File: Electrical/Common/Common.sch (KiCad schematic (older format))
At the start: 40 parts, among them J101 4PostTerm, J102 2PostTerm, J103 2PostTerm, J104 Conn_01x03, J105 01x02, J106 Conn_01x02, J107 01x04, J108 01x04, J109 01x04-1V8, J110 01x04-3v3, U101 ACS712ELCTR-05B-T, U102 ACS712ELCTR-05B-T, U103 LM2576HVS-ADJ, U104 LM2576HVS-ADJ

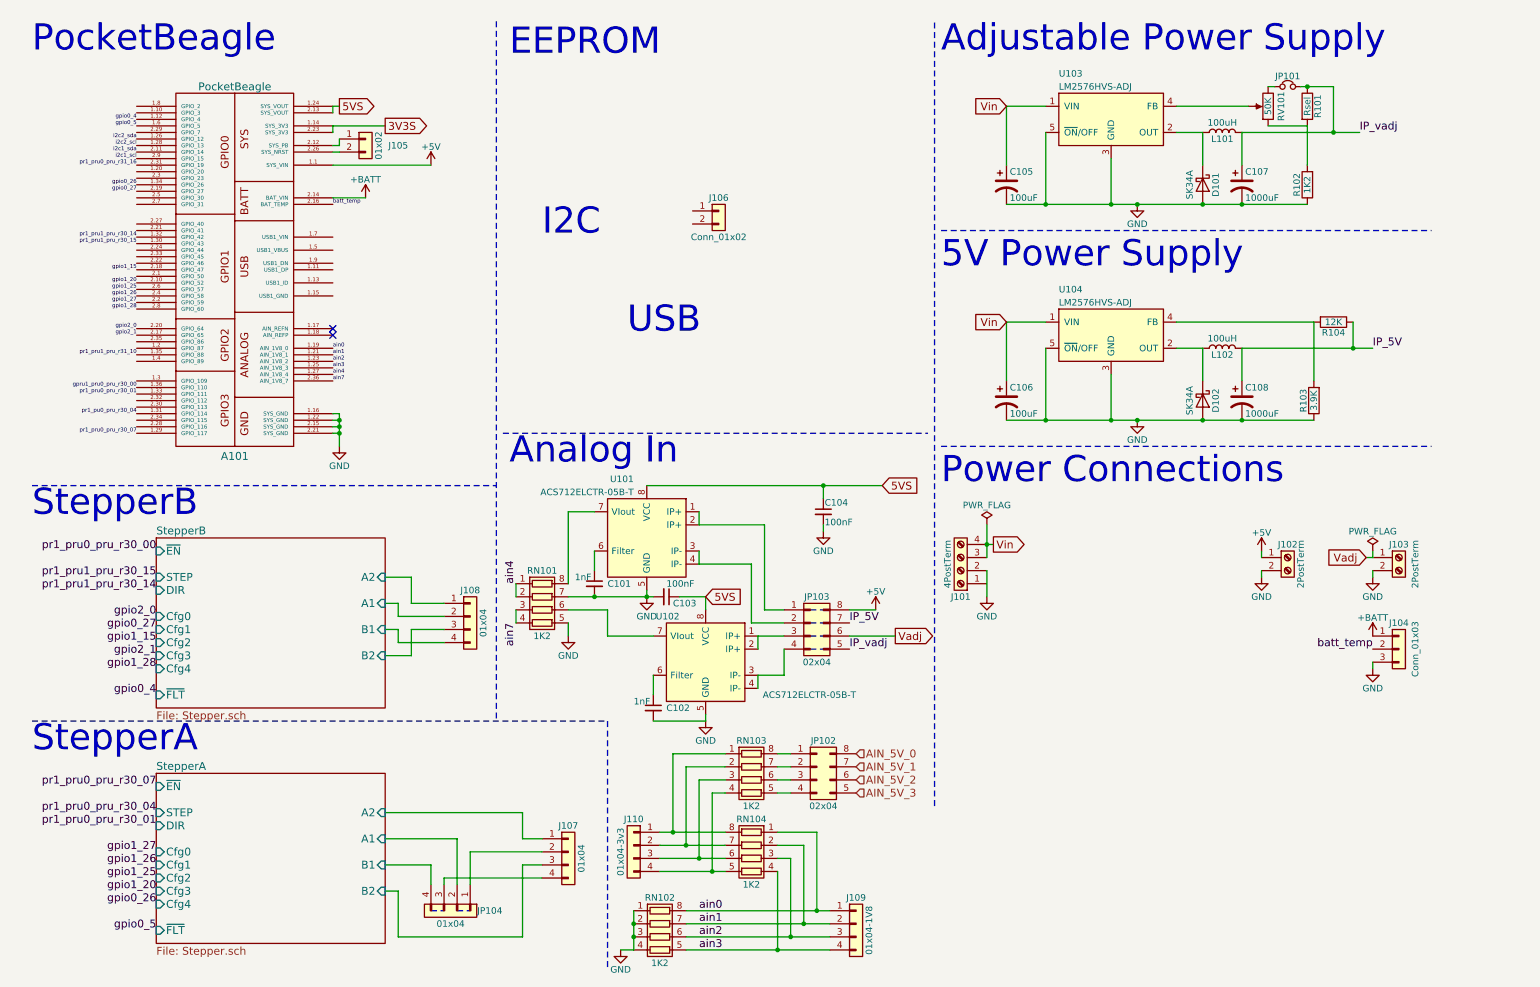
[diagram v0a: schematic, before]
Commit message: Completed components common to both quad and dual steppers (with the exception of power breakouts)
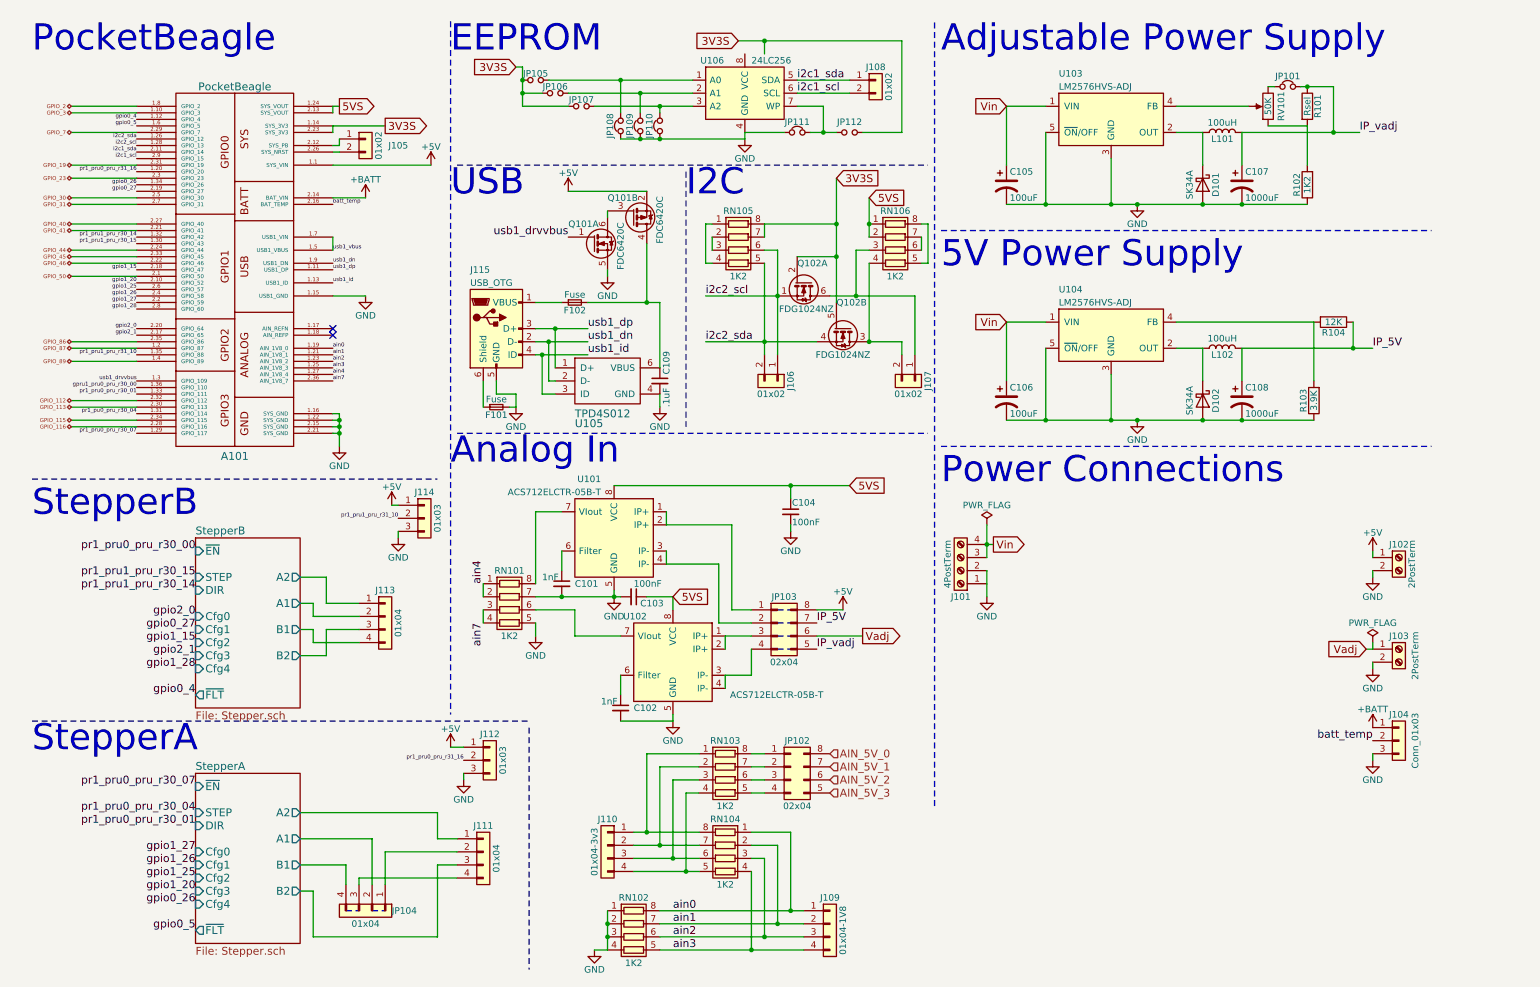
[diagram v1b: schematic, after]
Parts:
- added C109: .1uF, symbol C_Small
- added F101, F102: Fuse, symbol Fuse_Small
- added J107, J108: 01x02, symbol Conn_01x02
- added J112, J114: 01x03, symbol Conn_01x03
- added J115: USB_OTG, symbol USB_OTG
- added JP105, JP106, JP107, JP112: JPNO, symbol Jumper_NO_Small
- added JP108, JP109, JP110, JP111: JPNC, symbol Jumper_NC_Small
- added Q101: FDC6420C, TO_SOT_Packages_SMD:SOT-363_SC-70-6, symbol FDC6420C
- added Q102: FDG1024NZ, TO_SOT_Packages_SMD:SOT-363_SC-70-6, symbol FDG1024NZ
- added RN105, RN106: 1K2, symbol R_Pack04
- added U105: TPD4S012, symbol TPD4S012
- added U106: 24LC256, Housings_SOIC:SOIC-8_3.9x4.9mm_Pitch1.27mm, symbol 24LC256
- J106: value Conn_01x02 -> 01x02
- renumbered J107 to J111, J108 to J113
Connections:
- net +5V: now also J112.1 (Pin_1), J114.1 (Pin_1), Q101.2 (S)
- net 3V3S: now also JP105.1, JP106.1, JP107.1, JP112.2, Q102.2 (G), Q102.5 (G), RN105.7 (R2.2), RN105.8 (R1.2)
- net 5VS: now also RN106.1 (R1.1), RN106.2 (R2.1)
- net GND: now also A101.1.15 (USB1_GND), C109.2, F101.2, J112.3 (Pin_3), J114.3 (Pin_3), J115.5 (GND), JP108.1, JP109.1, JP110.1, JP111.1, Q101.5 (D), U105.4 (GND), U106.4 (GND)
- net i2c1_scl: now also J108.2 (Pin_2), U106.6 (SCL)
- net i2c1_sda: now also J108.1 (Pin_1), U106.5 (SDA)
- net i2c2_scl: now also J106.1 (Pin_1), Q102.1 (S), RN105.6 (R3.2)
- net i2c2_sda: now also J106.2 (Pin_2), Q102.4 (S), RN105.5 (R4.2)
- net pr1_pru0_pru_r31_16: now also A101.1.20 (GPIO_20), J112.2 (Pin_2); no longer A101.2.31 (GPIO_19)
- net pr1_pru1_pru_r31_10: now also J114.2 (Pin_2)
- net GPIO_3: now reaches A101.1.10 (GPIO_3)
- net usb1_dp: now reaches A101.1.11 (USB1_DP)
- net usb1_dp: now also J115.3 (D+), U105.1 (D+)
- net usb1_id: now reaches A101.1.13 (USB1_ID)
- net usb1_id: now also J115.4 (ID), U105.3 (ID)
- net GPIO_87: now reaches A101.1.2 (GPIO_87)
- net usb1_drvvbus: now reaches A101.1.3 (GPIO_109)
- net usb1_drvvbus: now also Q101.1 (G)
- net GPIO_89: now reaches A101.1.4 (GPIO_89)
- net usb1_vbus: now reaches A101.1.5 (USB1_VBUS)
- net usb1_vbus: now also A101.1.7 (USB1_VIN)
- net GPIO_2: now reaches A101.1.8 (GPIO_2)
- net usb1_dn: now reaches A101.1.9 (USB1_DN)
- net usb1_dn: now also J115.2 (D-), U105.2 (D-)
- net GPIO_50: now reaches A101.2.1 (GPIO_50)
- net GPIO_41: now reaches A101.2.21 (GPIO_41)
- net GPIO_46: now reaches A101.2.22 (GPIO_46)
- net GPIO_44: now reaches A101.2.24 (GPIO_44)
- net GPIO_40: now reaches A101.2.27 (GPIO_40)
- net GPIO_116: now reaches A101.2.28 (GPIO_116)
- net GPIO_7: now reaches A101.2.29 (GPIO_7)
- net GPIO_23: now reaches A101.2.3 (GPIO_23)
- net GPIO_113: now reaches A101.2.30 (GPIO_113)
- net GPIO_112: now reaches A101.2.32 (GPIO_112)
- net GPIO_45: now reaches A101.2.33 (GPIO_45)
- net GPIO_115: now reaches A101.2.34 (GPIO_115)
- net GPIO_86: now reaches A101.2.35 (GPIO_86)
- net GPIO_30: now reaches A101.2.5 (GPIO_30)
- net GPIO_31: now reaches A101.2.7 (GPIO_31)
- new net: JP105.2, JP108.2, U106.1 (A0)
- new net: JP106.2, JP109.2, U106.2 (A1)
- new net: JP107.2, JP110.2, U106.3 (A2)
- new net: JP111.2, JP112.1, U106.7 (WP)
- new net: J107.1 (Pin_1), Q102.6 (D), RN106.3 (R3.1)
- new net: J107.2 (Pin_2), Q102.3 (D), RN106.4 (R4.1)
- new net: RN105.1 (R1.1), RN105.4 (R4.1)
- new net: RN105.2 (R2.1), RN105.3 (R3.1)
- new net: RN106.5 (R4.2), RN106.8 (R1.2)
- new net: RN106.6 (R3.2), RN106.7 (R2.2)
- new net: F102.1, J115.1 (VBUS)
- new net: F101.1, J115.6 (Shield)
- new net: Q101.3 (G), Q101.6 (S)
- new net: C109.1, F102.2, Q101.4 (D), U105.6 (VBUS)
- new net GPIO_19: A101.2.31 (GPIO_19)
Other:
- moved on the sheet: C101, C102, C103, C104, J102, J103, J104, J106, J109, J110, J111, J113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

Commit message: Completed Schematic for Dual implementation
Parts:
- removed JP102, JP103: 02x04, symbol Conn_02x04_Counter_Clockwise
- removed U105: TPD4S012, symbol TPD4S012
- added JP208, JP209: 02x04, symbol Conn_02x04_Row_Letter_First
- added U201: TPD4S012, symbol TPD4S012
- C204: renamed from C109; value .1uF -> 100nF
- J207: renamed from J110; value 01x04-3v3 -> 01x04
- J209: renamed from J109; value 01x04-1V8 -> 01x04
- renumbered A101 to A201, C101 to C201, C102 to C202, C103 to C203, C104 to C205, C105 to C206, C106 to C207, C107 to C208, C108 to C209, D101 to D201, D102 to D202, F101 to F201, F102 to F202, J105 to J201, J113 to J202, J114 to J203, J111 to J204, J112 to J205, J115 to J206, J106 to J208, J108 to J210, J107 to J211, J101 to J212, J102 to J213, J103 to J214, J104 to J215, JP104 to JP201, JP105 to JP202, JP106 to JP203, JP107 to JP204, JP108 to JP205, JP109 to JP206, JP110 to JP207, JP111 to JP210, JP112 to JP211, JP101 to JP212, L101 to L201, L102 to L202, Q101 to Q201, Q102 to Q202, R101 to R201, R102 to R202, R103 to R203, R104 to R204, RN101 to RN201, RN102 to RN202, RN103 to RN203, RN104 to RN204, RN105 to RN205, RN106 to RN206, RV101 to RV201, U101 to U202, U102 to U203, U106 to U204, U103 to U205, U104 to U206
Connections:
- wire segments 236 -> 288
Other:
- note added: "1.8V"
- note added: "3.3V"
- note added: "5V"
- moved on the sheet: C204

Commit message: Completed quad schematics
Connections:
- wire segments 288 -> 238
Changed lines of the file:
@@
 LIBS:dc-dc
 LIBS:allegro
-LIBS:Dual-cache
+LIBS:Quad-cache
 EELAYER 25 0
 EELAYER END
 $Descr A4 11693 8268
 encoding utf-8
-Sheet 2 4
+Sheet 2 6
 Title ""
 Date ""
@@
 	2800 3500 2850 3500
 Wire Wire Line
-	2850 3500 2850 3550
-Wire Wire Line
-	2850 3550 2850 3600
-Wire Wire Line
-	2850 3600 2850 3650
-Wire Wire Line
-	2850 3650 2850 3750
+	2850 3500 2850 3750
 Wire Wire Line
 	2800 3550 2850 3550
@@
 Connection ~ 2850 3650
 Wire Wire Line
-	7950 1900 8250 1900
-Wire Wire Line
-	8250 1900 8750 1900
-Wire Wire Line
-	8750 1900 8950 1900
-Wire Wire Line
-	8950 1900 9450 1900
-Wire Wire Line
-	9450 1900 9750 1900
-Wire Wire Line
-	9750 1900 10250 1900
+	7950 1900 10250 1900
 Connection ~ 9450 1900
 Connection ~ 8950 1900
@@
 Connection ~ 8250 1900
 Wire Wire Line
-	7950 3550 8250 3550
-Wire Wire Line
-	8250 3550 8750 3550
-Wire Wire Line
-	8750 3550 8950 3550
-Wire Wire Line
-	8950 3550 9450 3550
-Wire Wire Line
-	9450 3550 9750 3550
-Wire Wire Line
-	9750 3550 10300 3550
+	7950 3550 10300 3550
 Connection ~ 9450 3550
 Connection ~ 8950 3550
@@
 	10300 2800 10300 3250
 Wire Wire Line
-	9750 3000 10600 3000
-Wire Wire Line
-	10600 3000 10750 3000
+	9750 3000 10750 3000
 Wire Wire Line
 	10600 3000 10600 2800
 Wire Wire Line
-	7800 4350 7800 4500
-Wire Wire Line
-	7800 4500 7800 4600
+	7800 4350 7800 4600
 Wire Wire Line
 	7800 4900 7800 4700
@@
 Connection ~ 10600 3000
 Wire Wire Line
-	9750 1350 10450 1350
-Wire Wire Line
-	10450 1350 10650 1350
+	9750 1350 10650 1350
 Connection ~ 9750 1900
 Wire Wire Line
@@
 	10250 1600 10250 1300
 Wire Wire Line
-	10200 1000 10250 1000
-Wire Wire Line
-	10250 1000 10450 1000
+	10200 1000 10450 1000
 Wire Wire Line
 	10450 1000 10450 1350
@@
 	5350 4350 5350 4250
 Wire Wire Line
-	4950 4050 6300 4050
-Wire Wire Line
-	6300 4050 6750 4050
+	4950 4050 6750 4050
 Wire Wire Line
 	5400 5000 5400 4900
@@
 	5500 6400 5500 7000
 Wire Wire Line
-	5100 7000 5500 7000
-Wire Wire Line
-	5500 7000 5600 7000
+	5100 7000 5600 7000
 Wire Wire Line
 	5600 6300 5400 6300
@@
 	5400 6300 5400 6900
 Wire Wire Line
-	5100 6900 5400 6900
-Wire Wire Line
-	5400 6900 5600 6900
+	5100 6900 5600 6900
 Wire Wire Line
 	5600 6200 5300 6200
@@
 	5300 6200 5300 6800
 Wire Wire Line
-	5100 6800 5300 6800
-Wire Wire Line
-	5300 6800 5600 6800
+	5100 6800 5600 6800
 Wire Wire Line
 	5600 6100 5200 6100
@@
 	5200 6100 5200 6700
 Wire Wire Line
-	5100 6700 5200 6700
-Wire Wire Line
-	5200 6700 5600 6700
+	5100 6700 5600 6700
 Connection ~ 5200 6700
 Connection ~ 5300 6800
@@
 	6000 7000 6000 7600
 Wire Wire Line
-	5300 7600 6000 7600
-Wire Wire Line
-	6000 7600 6400 7600
+	5300 7600 6400 7600
 Wire Wire Line
 	6000 6900 6100 6900
@@
 	6100 6900 6100 7500
 Wire Wire Line
-	5300 7500 6100 7500
-Wire Wire Line
-	6100 7500 6400 7500
+	5300 7500 6400 7500
 Wire Wire Line
 	6000 6800 6200 6800
@@
 	6200 6800 6200 7400
 Wire Wire Line
-	5300 7400 6200 7400
-Wire Wire Line
-	6200 7400 6400 7400
+	5300 7400 6400 7400
 Wire Wire Line
 	6000 6700 6300 6700
@@
 	6300 6700 6300 7300
 Wire Wire Line
-	5300 7300 6300 7300
-Wire Wire Line
-	6300 7300 6400 7300
+	5300 7300 6400 7300
 Connection ~ 6300 7300
 Connection ~ 6200 7400
@@
 Connection ~ 6000 7600
 Wire Wire Line
-	4900 7300 4900 7400
-Wire Wire Line
-	4900 7400 4900 7500
-Wire Wire Line
-	4900 7500 4900 7600
+	4900 7300 4900 7600
 Connection ~ 4900 7400
 Connection ~ 4900 7500
 Wire Wire Line
-	4350 4900 4550 4900
-Wire Wire Line
-	4550 4900 4950 4900
-Wire Wire Line
-	4950 4900 5000 4900
+	4350 4900 5000 4900
 Wire Wire Line
 	5400 5850 5000 5850
@@
 	6100 750  6100 650
 Wire Wire Line
-	5900 650  6100 650
-Wire Wire Line
-	6100 650  7150 650
+	5900 650  7150 650
 Wire Wire Line
 	5950 1400 5950 1350
@@
 	5950 1350 6250 1350
 Wire Wire Line
-	6450 1350 6550 1350
-Wire Wire Line
-	6550 1350 6650 1350
+	6450 1350 6650 1350
 Wire Wire Line
 	6850 1350 7150 1350
@@
 Connection ~ 6550 1350
 Wire Wire Line
-	5000 1400 5150 1400
-Wire Wire Line
-	5150 1400 5300 1400
-Wire Wire Line
-	5300 1400 5950 1400
-Wire Wire Line
-	4800 1150 5300 1150
-Wire Wire Line
-	5300 1150 5550 1150
+	5000 1400 5950 1400
+Wire Wire Line
+	4800 1150 5550 1150
 Wire Wire Line
 	5300 1150 5300 1200
@@
 	5150 1200 5150 1050
 Wire Wire Line
-	4600 1050 5150 1050
-Wire Wire Line
-	5150 1050 5550 1050
+	4600 1050 5550 1050
 Connection ~ 5150 1400
 Wire Wire Line
 	5000 1200 5000 950
 Wire Wire Line
-	4450 950  5000 950
-Wire Wire Line
-	5000 950  5550 950
+	4450 950  5550 950
 Connection ~ 5300 1150
 Connection ~ 5150 1050
 Connection ~ 5000 950
 Wire Wire Line
-	4250 850  4250 950
-Wire Wire Line
-	4250 950  4250 1050
-Wire Wire Line
-	4250 1050 4250 1150
+	4250 850  4250 1150
 Wire Wire Line
 	4250 850  4200 850
@@
 	7350 2350 7300 2350
 Wire Wire Line
-	6900 1850 6900 2050
-Wire Wire Line
-	6900 2050 6900 2150
+	6900 1850 6900 2150
 Connection ~ 6900 2050
 Wire Wire Line
@@
 Connection ~ 6900 2950
 Wire Wire Line
-	6600 2600 6800 2600
-Wire Wire Line
-	6800 2600 7250 2600
+	6600 2600 7250 2600
 Wire Wire Line
 	7250 2600 7250 3050
 Wire Wire Line
-	6650 1700 6650 2050
-Wire Wire Line
-	6650 2050 6650 2300
-Wire Wire Line
-	6650 2300 6650 2650
+	6650 1700 6650 2650
 Wire Wire Line
 	6350 2300 6650 2300
@@
 	6100 2250 6200 2250
 Wire Wire Line
-	6200 2250 6200 2600
-Wire Wire Line
-	6200 2600 6200 3050
-Wire Wire Line
-	6100 2350 6100 2950
-Wire Wire Line
-	6100 2950 6100 3050
-Wire Wire Line
-	5650 2950 6100 2950
-Wire Wire Line
-	6100 2950 6500 2950
+	6200 2250 6200 3050
+Wire Wire Line
+	6100 2350 6100 3050
+Wire Wire Line
+	5650 2950 6500 2950
 Connection ~ 6200 2600
 Wire Wire Line
@@
 	4350 2650 4550 2650
 Wire Wire Line
-	4750 2650 5200 2650
-Wire Wire Line
-	5200 2650 5300 2650
+	4750 2650 5300 2650
 Wire Wire Line
 	3950 3250 3950 3450
@@
 	4050 3350 4050 3250
 Wire Wire Line
-	4350 3050 4400 3050
-Wire Wire Line
-	4400 3050 4750 3050
+	4350 3050 4750 3050
 Wire Wire Line
 	5300 2650 5300 3150
 Connection ~ 5200 2650
 Wire Wire Line
-	4350 2950 4450 2950
-Wire Wire Line
-	4450 2950 4750 2950
-Wire Wire Line
-	4350 2850 4500 2850
-Wire Wire Line
-	4500 2850 4750 2850
+	4350 2950 4750 2950
+Wire Wire Line
+	4350 2850 4750 2850
 $Comp
 L C_Small C204
@@
 Wire Wire Line
 	3800 6300 3800 6250
-Text Label 3800 6150 2    30   ~ 0
+Text Label 3800 6150 2    60   ~ 0
 pr1_pru0_pru_r31_16
-Text Label 3300 4300 2    30   ~ 0
+Text Label 3300 4300 2    60   ~ 0
 pr1_pru1_pru_r31_10
 $Comp

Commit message: Fixed DRC errors
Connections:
- net labels removed: gpru1_pru0_pru_r30_00, pr1_pu0_pru_r30_04
- wire segments 238 -> 240
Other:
- moved on the sheet: J201

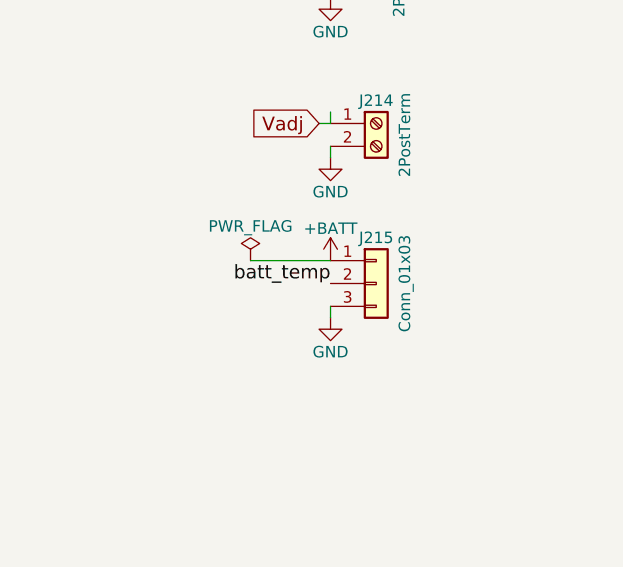
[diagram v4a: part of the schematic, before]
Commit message: Associated footprints. Added some footprint libraries to support.
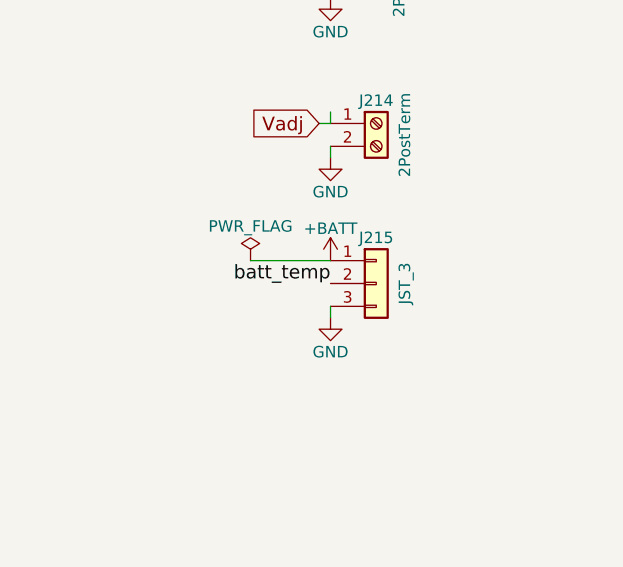
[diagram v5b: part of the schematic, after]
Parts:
- A201: footprint (none) -> footprints:PocketBeagle
- C201, C202, C203, C204, C205: footprint (none) -> Capacitors_SMD:C_0603_HandSoldering
- C206, C207, C208, C209: footprint (none) -> Capacitors_SMD:CP_Elec_8x10
- D201, D202: footprint (none) -> Diodes_SMD:D_SMB-SMC_Universal_Handsoldering
- F201, F202: footprint (none) -> SMD_Packages:SMD-1206_Pol
- J201, J208, J210, J211: footprint (none) -> Socket_Strips:Socket_Strip_Straight_1x02_Pitch2.54mm
- J202, J204, J207, J209, JP201: footprint (none) -> Socket_Strips:Socket_Strip_Straight_1x04_Pitch2.54mm
- J203, J205: footprint (none) -> Socket_Strips:Socket_Strip_Straight_1x03_Pitch2.54mm
- J206: footprint (none) -> Connectors_USB:USB_Micro-B_Molex-105017-0001
- J212: footprint (none) -> footprints:TerminalBlock_Custom_1x04P5.08mm
- J213, J214: footprint (none) -> footprints:TerminalBlock_Custom_1x02.54mm
- J215: value Conn_01x03 -> JST_3; footprint (none) -> Connectors_JST:JST_XH_B03B-XH-A_03x2.50mm_Straight
- JP202, JP203, JP204, JP211: footprint (none) -> footprints:JPNO
- JP205, JP206, JP207, JP210: footprint (none) -> footprints:JPNC
- JP208, JP209: footprint (none) -> Socket_Strips:Socket_Strip_Straight_2x04_Pitch2.54mm
- JP212: value Jumper -> JPNC; footprint (none) -> footprints:JPNC
- L201, L202: footprint (none) -> footprints:BOURNS-SRN1060
- R201, R202, R203, R204: footprint (none) -> Resistors_SMD:R_0603_HandSoldering
- RN201, RN202, RN203, RN204, RN205, RN206: footprint (none) -> footprints:R_Array_1206x04
- RV201: footprint (none) -> Potentiometers:Potentiometer_Trimmer-EVM3E
- U201: footprint (none) -> Housings_SON:WSON6_1.5x1.5mm_Pitch0.5mm
- U204: footprint Housings_SOIC:SOIC-8_3.9x4.9mm_Pitch1.27mm -> Housings_DIP:DIP-8_W7.62mm
